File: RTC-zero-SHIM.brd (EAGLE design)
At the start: 30 x 65 mm, 16 parts, among them IC1 DS3231/SO, IC2 DS3231M

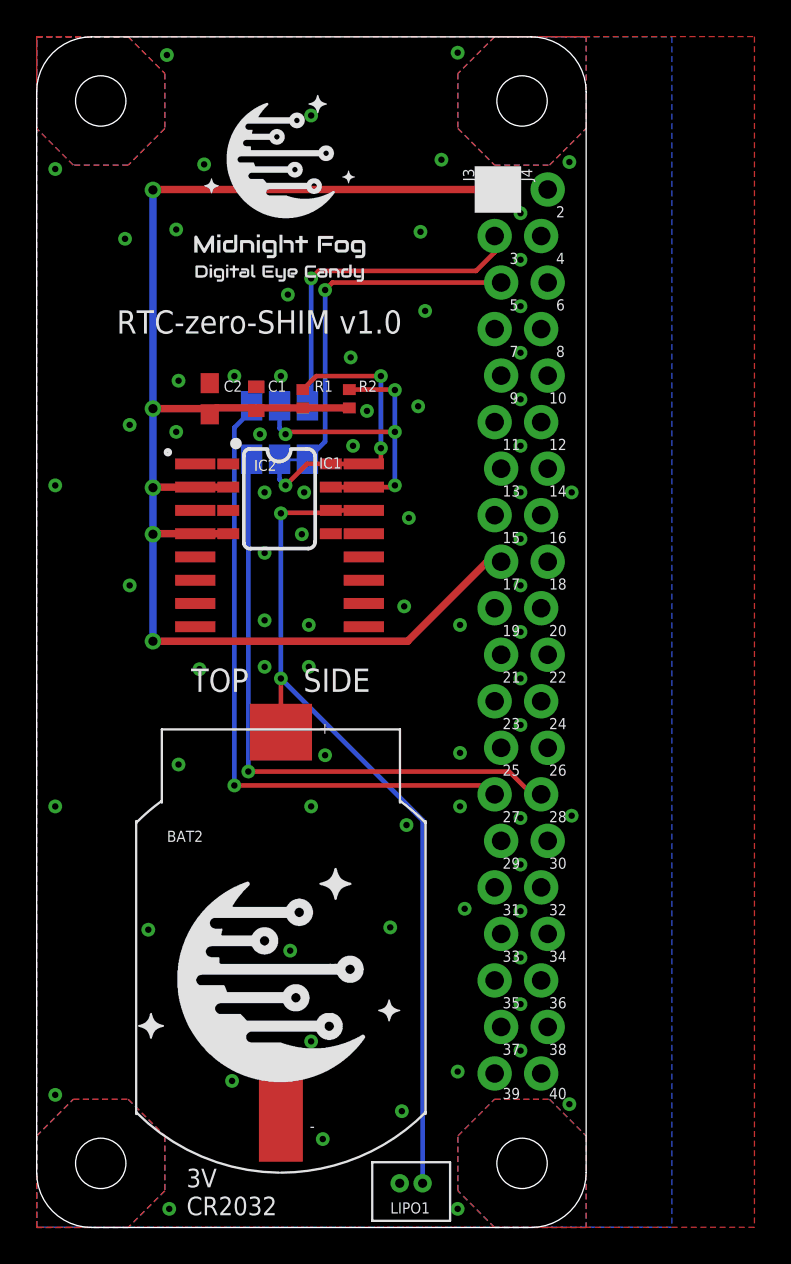
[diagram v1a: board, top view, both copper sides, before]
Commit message: Added second batter holder as alternative. Generated CAM. Generated PDF schematics. Generated PNG preview image.
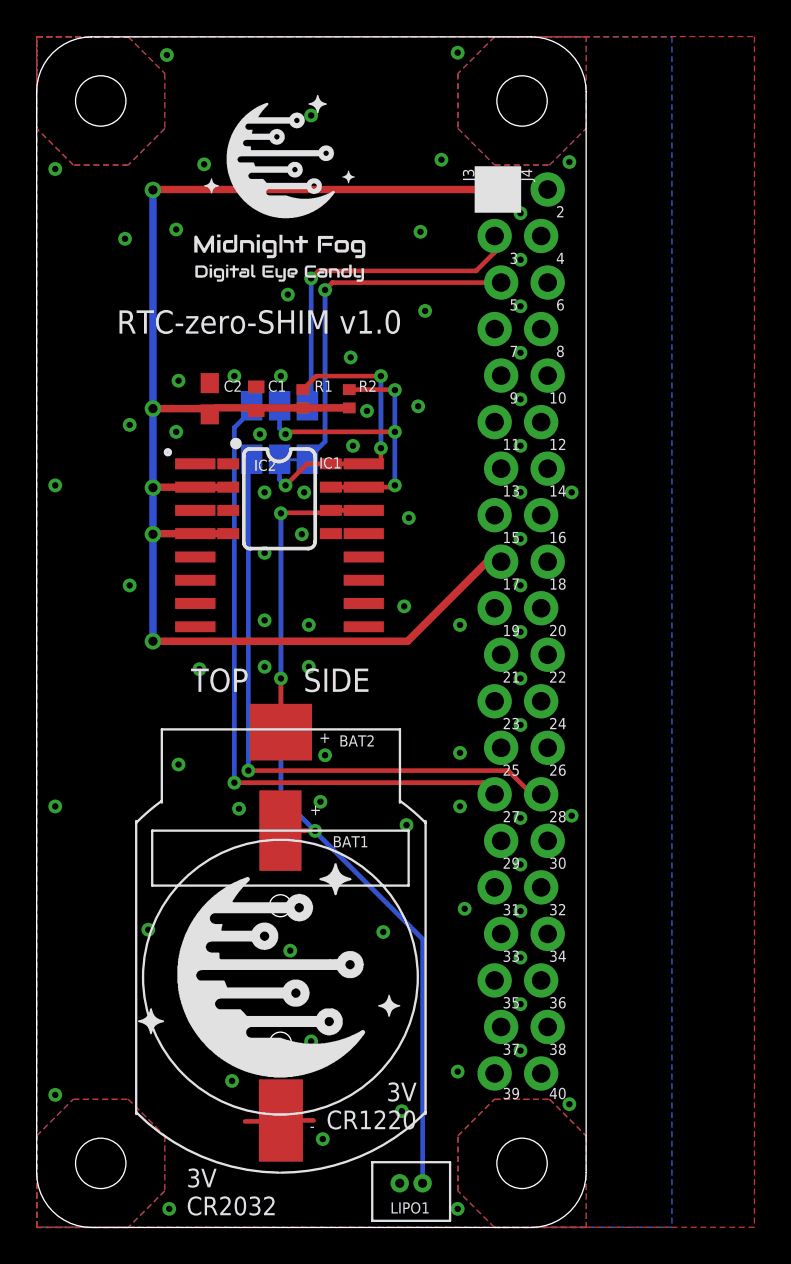
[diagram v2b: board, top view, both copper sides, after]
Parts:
- added BAT1: CR1220-2, CR1220-2:CR1220-2
- moved LOGO4 0.25 mm to (4.75, 7.27)
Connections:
- net GND: now also BAT1.BAT-
- net VBAT: now also BAT1.BAT+
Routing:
- net GND: track 0.00 -> 3.86 mm, vias 76 -> 77
- net VBAT: track 47.3 -> 49.2 mm, vias 2 -> 3
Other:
- board text added: "3V CR1220"
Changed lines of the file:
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@@
 CR2032</text>
 <circle x="7.165" y="42.322" radius="0.127" width="0.2032" layer="21"/>
-<text x="15.42" y="26.955" size="0.6096" layer="21" font="vector" ratio="12">+</text>
+<text x="15.42" y="26.447" size="0.6096" layer="21" font="vector" ratio="12">+</text>
 <text x="14.912" y="5.238" size="0.6096" layer="21" font="vector" ratio="12">-</text>
 <text x="19.357" y="48.164" size="1.016" layer="22" font="vector" ratio="12" rot="MR0">(c) Andriy Golovnya</text>
@@
 <text x="25.436" y="7.01" size="0.6096" layer="21" font="vector" ratio="12">39</text>
 <text x="27.976" y="7.01" size="0.6096" layer="21" font="vector" ratio="12">40</text>
+<text x="14.912" y="22.51" size="0.6096" layer="21" font="vector" ratio="12">+</text>
+<text x="20.754" y="5.365" size="1.016" layer="21" font="vector" ratio="12" align="bottom-right">3V
+CR1220</text>
 </plain>
 <attributes>
@@
 </element>
 <element name="BAT2" library="BS-8-1" package="BS-8-1" value="BS-8-1" x="13.335" y="14.192" smashed="yes" rot="R180">
-<attribute name="NAME" x="7.112" y="21.05" size="0.6096" layer="25" font="vector"/>
-<attribute name="VALUE" x="7.112" y="19.907" size="0.6096" layer="27" font="vector"/>
+<attribute name="NAME" x="16.51" y="26.257" size="0.6096" layer="25" font="vector"/>
+<attribute name="VALUE" x="16.51" y="25.368" size="0.6096" layer="27" font="vector"/>
 </element>
 <element name="LOGO1" library="_my_logos" package="MFDEC_SQ_8MM" value="MFDECLOGO_SQ_8MM" x="7.927" y="51.339" smashed="yes"/>
@@
 <attribute name="VALUE" x="14.785" y="38.004" size="0.6096" layer="27" font="vector" rot="R90"/>
 </element>
-<element name="LOGO4" library="_my_logos" package="MFDEC_L_10MM" value="MFDECLOGO_L_10MM" x="4.752" y="7.016" smashed="yes"/>
+<element name="LOGO4" library="_my_logos" package="MFDEC_L_10MM" value="MFDECLOGO_L_10MM" x="4.752" y="7.27" smashed="yes"/>
+<element name="BAT1" library="CR1220-2" package="CR1220-2" value="CR1220-2" x="13.3096" y="13.6652" smashed="yes" rot="R180">
+<attribute name="NAME" x="16.1544" y="20.7518" size="0.6096" layer="25" font="vector"/>
+<attribute name="VALUE" x="16.1544" y="19.7358" size="0.6096" layer="27" font="vector"/>
+</element>
 </elements>
 <signals>
@@
 <wire x1="15.934" y1="39.02" x2="16.061" y2="39.147" width="0.254" layer="1"/>
 <wire x1="15.934" y1="39.02" x2="13.366" y2="39.02" width="0.254" layer="1"/>
-<wire x1="21.072" y1="2.413" x2="21.072" y2="22.235" width="0.254" layer="16"/>
-<wire x1="21.072" y1="22.235" x2="13.335" y2="29.972" width="0.254" layer="16"/>
+<wire x1="15.2046" y1="21.6508" x2="15.2046" y2="21.6154" width="0.254" layer="16"/>
+<wire x1="21.072" y1="2.413" x2="21.072" y2="15.748" width="0.254" layer="16"/>
+<wire x1="21.072" y1="15.748" x2="15.2046" y2="21.6154" width="0.254" layer="16"/>
+<wire x1="15.2046" y1="21.6508" x2="13.335" y2="23.5204" width="0.254" layer="16"/>
+<wire x1="13.335" y1="23.5204" x2="13.335" y2="29.972" width="0.254" layer="16"/>
+<contactref element="BAT1" pad="BAT+"/>
+<wire x1="13.3096" y1="21.6652" x2="15.1902" y2="21.6652" width="0.254" layer="1"/>
+<wire x1="15.1902" y1="21.6652" x2="15.2046" y2="21.6508" width="0.254" layer="1"/>
+<via x="15.2046" y="21.6508" extent="1-16" drill="0.35"/>
 </signal>
 <signal name="SCL">
@@
 <via x="8.89" y="30.48" extent="1-16" drill="0.35"/>
 <via x="7.747" y="25.273" extent="1-16" drill="0.35"/>
-<via x="14.986" y="22.987" extent="1-16" drill="0.35"/>
+<via x="15.494" y="23.241" extent="1-16" drill="0.35"/>
 <via x="15.748" y="25.781" extent="1-16" drill="0.35"/>
 <via x="23.114" y="22.987" extent="1-16" drill="0.35"/>
@@
 <via x="14.986" y="60.706" extent="1-16" drill="0.35"/>
 <via x="6.096" y="16.256" extent="1-16" drill="0.35"/>
-<via x="19.304" y="16.383" extent="1-16" drill="0.35"/>
+<via x="18.923" y="16.129" extent="1-16" drill="0.35"/>
 <via x="22.987" y="8.509" extent="1-16" drill="0.35"/>
 <via x="23.368" y="17.399" extent="1-16" drill="0.35"/>
 <via x="20.193" y="21.971" extent="1-16" drill="0.35"/>
 <via x="13.843" y="15.113" extent="1-16" drill="0.35"/>
+<contactref element="BAT1" pad="BAT-"/>
+<via x="11.049" y="22.86" extent="1-16" drill="0.35"/>
+<wire x1="13.3096" y1="5.6652" x2="13.4864" y2="5.842" width="0.254" layer="1"/>
+<wire x1="13.4864" y1="5.842" x2="15.113" y2="5.842" width="0.254" layer="1"/>
+<wire x1="13.3096" y1="5.6652" x2="13.1826" y2="5.7922" width="0.254" layer="1"/>
+<wire x1="13.1826" y1="5.7922" x2="11.3802" y2="5.7922" width="0.254" layer="1"/>
 </signal>
 <signal name="SCL0">
@@
 <contactref element="SJ2" pad="3"/>
 <wire x1="27.5442" y1="23.647" x2="27.0362" y2="23.647" width="0.254" layer="1"/>
-<wire x1="27.0362" y1="23.647" x2="25.7912" y2="24.892" width="0.254" layer="1"/>
-<wire x1="25.7912" y1="24.892" x2="11.557" y2="24.892" width="0.254" layer="1"/>
-<via x="11.557" y="24.892" extent="1-16" drill="0.35"/>
-<wire x1="11.557" y1="24.892" x2="11.557" y2="41.761" width="0.254" layer="16"/>
+<wire x1="27.0362" y1="23.647" x2="25.7404" y2="24.9428" width="0.254" layer="1"/>
+<wire x1="25.7404" y1="24.9428" x2="11.557" y2="24.9428" width="0.254" layer="1"/>
+<via x="11.557" y="24.9428" extent="1-16" drill="0.35"/>
+<wire x1="11.557" y1="24.9428" x2="11.557" y2="41.761" width="0.254" layer="16"/>
 <wire x1="11.557" y1="41.761" x2="11.737" y2="41.941" width="0.254" layer="16"/>
 </signal>
@@
 <wire x1="11.737" y1="44.862" x2="11.737" y2="44.608" width="0.254" layer="16"/>
 <wire x1="11.737" y1="44.608" x2="10.795" y2="43.666" width="0.254" layer="16"/>
-<wire x1="10.795" y1="43.666" x2="10.795" y2="24.13" width="0.254" layer="16"/>
-<via x="10.795" y="24.13" extent="1-16" drill="0.35"/>
-<wire x1="10.795" y1="24.13" x2="24.5212" y2="24.13" width="0.254" layer="1"/>
-<wire x1="24.5212" y1="24.13" x2="25.0042" y2="23.647" width="0.254" layer="1"/>
+<wire x1="10.795" y1="43.666" x2="10.795" y2="24.2824" width="0.254" layer="16"/>
+<via x="10.795" y="24.2824" extent="1-16" drill="0.35"/>
+<wire x1="10.795" y1="24.2824" x2="24.3688" y2="24.2824" width="0.254" layer="1"/>
+<wire x1="24.3688" y1="24.2824" x2="25.0042" y2="23.647" width="0.254" layer="1"/>
 </signal>
 <signal name="SDA1">
